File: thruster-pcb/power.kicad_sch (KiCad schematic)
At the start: 18 parts, among them J301 Molex_Pico-SPOX_Horizontal, J302 Molex_Pico-Lock-PLUS_Vertical, M301 Fan_5VDC_25x25x8mm, Q301 MOSFET-N-CH, U301 Switching_5V_500mA, U302 Linear_3.3V_1A

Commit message: tmc5160-usb -> thruster-pcb
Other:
- title: tmc5160-usb -> thruster-pcb
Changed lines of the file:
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@@
   (paper "A4")
   (title_block
-    (title "tmc5160-usb")
+    (title "thruster-pcb")
     (date "2024-05-10")
     (rev "1.0")
@@
     (pin "1")
     (instances
-      (project "tmc5160-usb"
+      (project "thruster-pcb"
         (path "/df2b2e89-e055-4140-95de-f1df723db034/c1dd8f61-494c-402f-8e59-08309c64fc3f"
           (reference "D303") (unit 1)
@@
     (pin "7")
     (instances
-      (project "tmc5160-usb"
+      (project "thruster-pcb"
         (path "/df2b2e89-e055-4140-95de-f1df723db034/c1dd8f61-494c-402f-8e59-08309c64fc3f"
           (reference "U302") (unit 1)
@@
     (pin "1")
     (instances
-      (project "tmc5160-usb"
+      (project "thruster-pcb"
         (path "/df2b2e89-e055-4140-95de-f1df723db034/c1dd8f61-494c-402f-8e59-08309c64fc3f"
           (reference "#FLG0303") (unit 1)
@@
     (pin "1")
     (instances
-      (project "tmc5160-usb"
+      (project "thruster-pcb"
         (path "/df2b2e89-e055-4140-95de-f1df723db034/c1dd8f61-494c-402f-8e59-08309c64fc3f"
           (reference "J302") (unit 1)
@@
     (pin "1")
     (instances
-      (project "tmc5160-usb"
+      (project "thruster-pcb"
         (path "/df2b2e89-e055-4140-95de-f1df723db034/c1dd8f61-494c-402f-8e59-08309c64fc3f"
           (reference "C302") (unit 1)
@@
     (pin "1")
     (instances
-      (project "tmc5160-usb"
+      (project "thruster-pcb"
         (path "/df2b2e89-e055-4140-95de-f1df723db034/c1dd8f61-494c-402f-8e59-08309c64fc3f"
           (reference "L301") (unit 1)
@@
     (pin "1")
     (instances
-      (project "tmc5160-usb"
+      (project "thruster-pcb"
         (path "/df2b2e89-e055-4140-95de-f1df723db034/c1dd8f61-494c-402f-8e59-08309c64fc3f"
           (reference "R303") (unit 1)
@@
     (pin "1")
     (instances
-      (project "tmc5160-usb"
+      (project "thruster-pcb"
         (path "/df2b2e89-e055-4140-95de-f1df723db034/c1dd8f61-494c-402f-8e59-08309c64fc3f"
           (reference "J301") (unit 1)
@@
     (pin "1")
     (instances
-      (project "tmc5160-usb"
+      (project "thruster-pcb"
         (path "/df2b2e89-e055-4140-95de-f1df723db034/c1dd8f61-494c-402f-8e59-08309c64fc3f"
           (reference "C304") (unit 1)
@@
     (pin "1")
     (instances
-      (project "tmc5160-usb"
+      (project "thruster-pcb"
         (path "/df2b2e89-e055-4140-95de-f1df723db034/c1dd8f61-494c-402f-8e59-08309c64fc3f"
           (reference "C301") (unit 1)
@@
     (pin "1")
     (instances
-      (project "tmc5160-usb"
+      (project "thruster-pcb"
         (path "/df2b2e89-e055-4140-95de-f1df723db034/c1dd8f61-494c-402f-8e59-08309c64fc3f"
           (reference "D301") (unit 1)
@@
     (pin "1")
     (instances
-      (project "tmc5160-usb"
+      (project "thruster-pcb"
         (path "/df2b2e89-e055-4140-95de-f1df723db034/c1dd8f61-494c-402f-8e59-08309c64fc3f"
           (reference "D302") (unit 1)
@@
     (pin "1")
     (instances
-      (project "tmc5160-usb"
+      (project "thruster-pcb"
         (path "/df2b2e89-e055-4140-95de-f1df723db034/c1dd8f61-494c-402f-8e59-08309c64fc3f"
           (reference "C305") (unit 1)
@@
     (pin "1")
     (instances
-      (project "tmc5160-usb"
+      (project "thruster-pcb"
         (path "/df2b2e89-e055-4140-95de-f1df723db034/c1dd8f61-494c-402f-8e59-08309c64fc3f"
           (reference "#FLG0302") (unit 1)
@@
     (pin "2")
     (instances
-      (project "tmc5160-usb"
+      (project "thruster-pcb"
         (path "/df2b2e89-e055-4140-95de-f1df723db034/c1dd8f61-494c-402f-8e59-08309c64fc3f"
           (reference "R302") (unit 1)
@@
     (pin "1")
     (instances
-      (project "tmc5160-usb"
+      (project "thruster-pcb"
         (path "/df2b2e89-e055-4140-95de-f1df723db034/c1dd8f61-494c-402f-8e59-08309c64fc3f"
           (reference "#FLG0301") (unit 1)
@@
     (pin "1")
     (instances
-      (project "tmc5160-usb"
+      (project "thruster-pcb"
         (path "/df2b2e89-e055-4140-95de-f1df723db034/c1dd8f61-494c-402f-8e59-08309c64fc3f"
           (reference "R301") (unit 1)
@@
     (pin "4")
     (instances
-      (project "tmc5160-usb"
+      (project "thruster-pcb"
         (path "/df2b2e89-e055-4140-95de-f1df723db034/c1dd8f61-494c-402f-8e59-08309c64fc3f"
           (reference "U301") (unit 1)
@@
     (pin "3")
     (instances
-      (project "tmc5160-usb"
+      (project "thruster-pcb"
         (path "/df2b2e89-e055-4140-95de-f1df723db034/c1dd8f61-494c-402f-8e59-08309c64fc3f"
           (reference "Q301") (unit 1)
@@
     (pin "2")
     (instances
-      (project "tmc5160-usb"
+      (project "thruster-pcb"
         (path "/df2b2e89-e055-4140-95de-f1df723db034/c1dd8f61-494c-402f-8e59-08309c64fc3f"
           (reference "M301") (unit 1)
@@
     (pin "1")
     (instances
-      (project "tmc5160-usb"
+      (project "thruster-pcb"
         (path "/df2b2e89-e055-4140-95de-f1df723db034/c1dd8f61-494c-402f-8e59-08309c64fc3f"
           (reference "C303") (unit 1)

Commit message: Add reference files
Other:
- company: Howard Hughes Medical Institute -> Mechatronic Magic
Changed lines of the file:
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@@
   (title_block
     (title "thruster-pcb")
-    (date "2024-05-10")
+    (date "2025-01-04")
     (rev "1.0")
-    (company "Howard Hughes Medical Institute")
+    (company "Mechatronic Magic")
   )
   (no_connect (at 163.83 68.58))

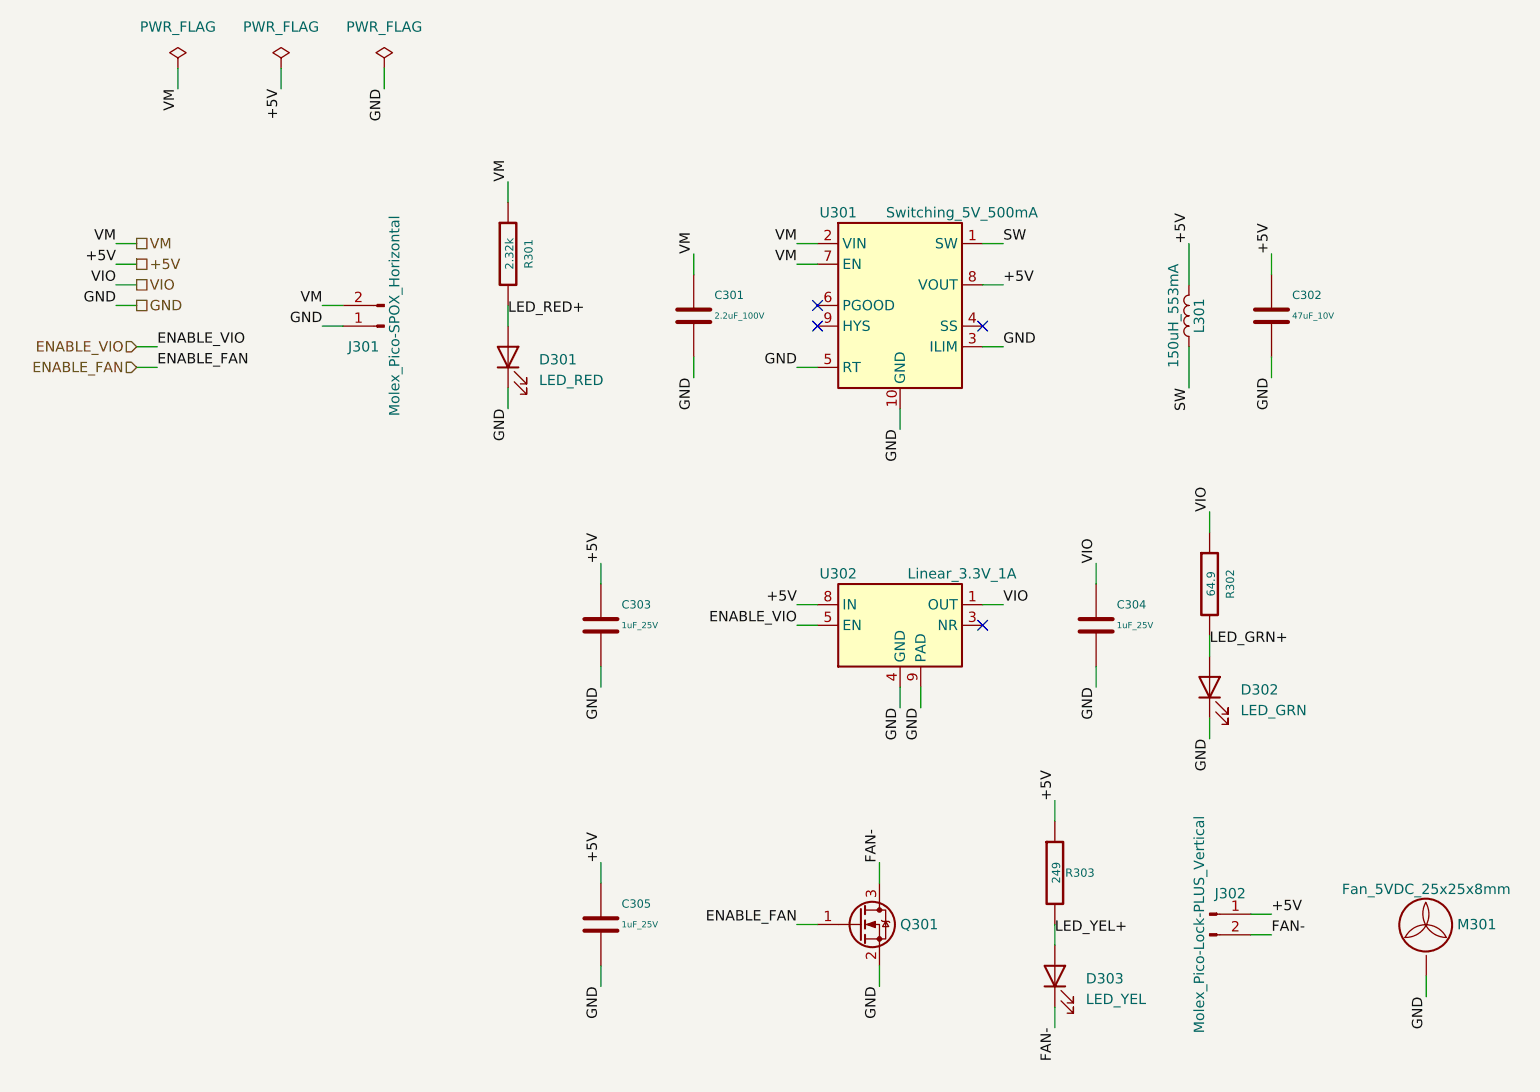
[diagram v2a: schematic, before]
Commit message: Use PCA9685 and nRF52
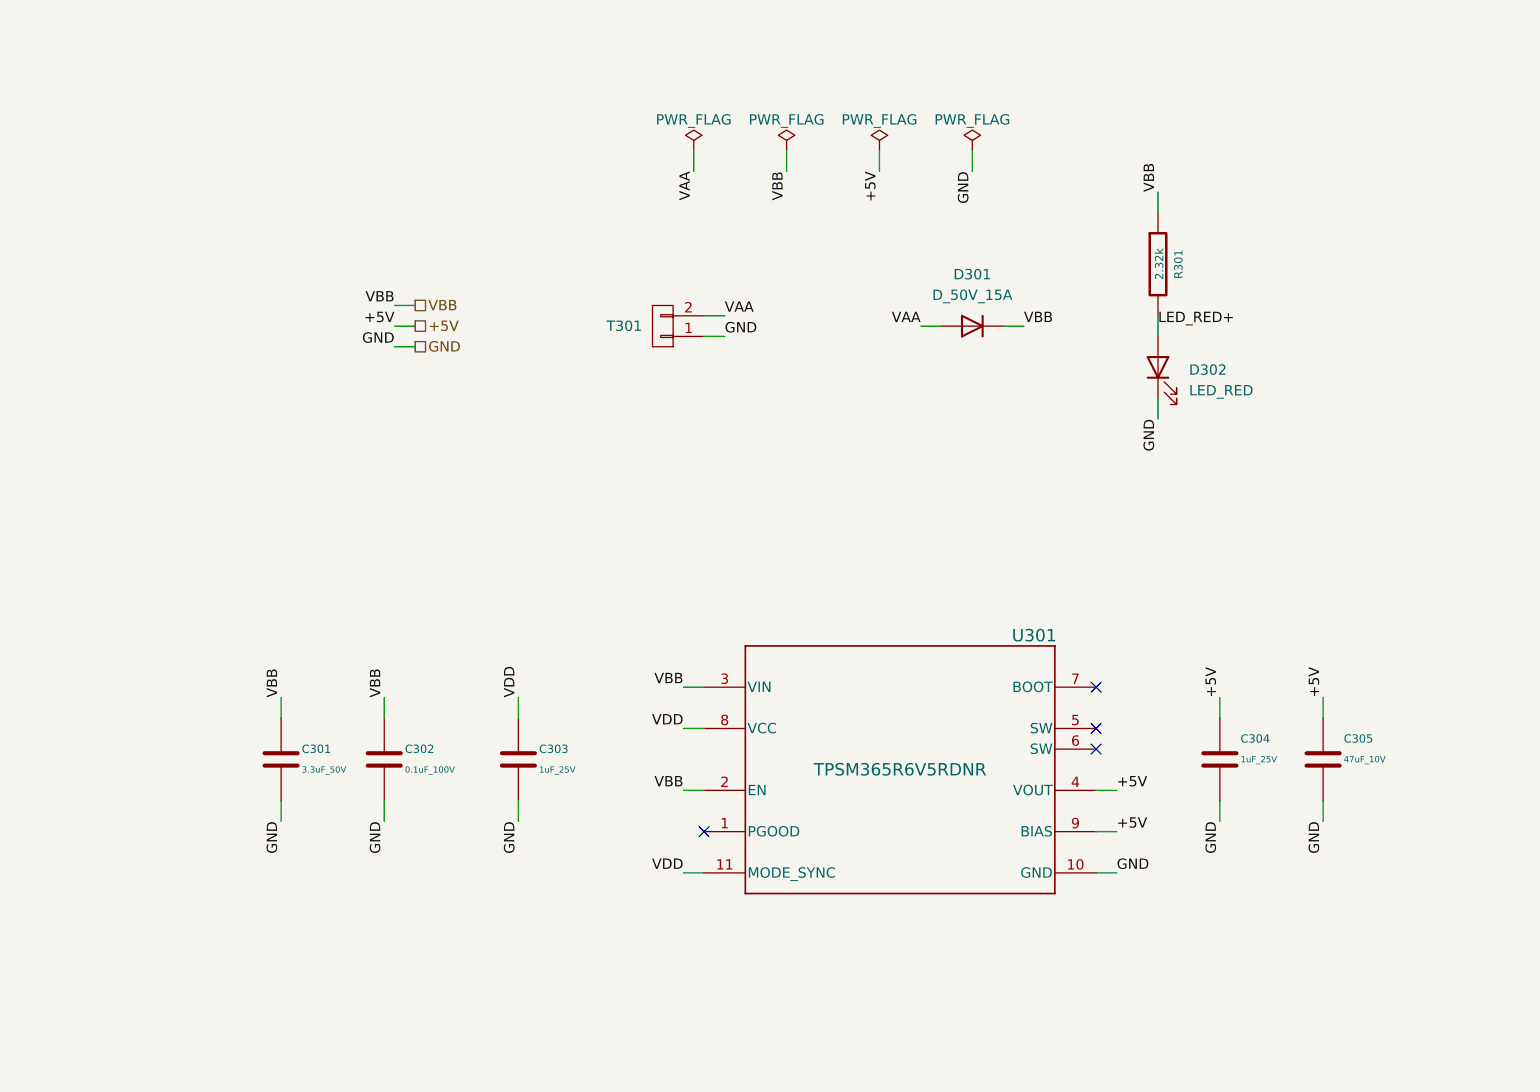
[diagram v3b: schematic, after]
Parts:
- removed C301: 2.2uF_100V, Janelia:C_0805_2012Metric, symbol Janelia:C_2.2uF_100V_0805
- removed C302: 47uF_10V, Janelia:C_0805_2012Metric, symbol Janelia:C_47uF_10V_0805
- removed C305: 1uF_25V, Janelia:C_0402_1005Metric, symbol Janelia:C_1uF_25V_0402
- removed D301: LED_RED, Janelia:LED_0402-1005_KNB, symbol Janelia:LED_KNB_20mA_RED_1.95V_0402
- removed D302: LED_GRN, Janelia:LED_0402-1005_KNB, symbol Janelia:LED_KNB_20mA_GRN_2.1V_0402
- removed D303: LED_YEL, Janelia:LED_0402-1005_KNB, symbol Janelia:LED_KNB_20mA_YEL_2V_0402
- removed J301: Molex_Pico-SPOX_Horizontal, Janelia:Molex_Pico-SPOX-87438_1x02-P1.5mm_Horizontal, symbol Janelia:Conn_01x02_P1.5mm_Molex_Pico-SPOX-87438_Horizontal
- removed J302: Molex_Pico-Lock-PLUS_Vertical, Janelia:Molex_Micro-Lock-PLUS-505568_1x02_P1.25mm_Vertical, symbol Janelia:Conn_01x02_P1.25mm_Molex_Micro-Lock-PLUS-505568_Vertical
- removed L301: 150uH_553mA, Janelia:IND_CB_SD25, symbol Janelia:L_150uH_553mA
- removed M301: Fan_5VDC_25x25x8mm, Janelia:FAN_5VDC_25x25x8mm, symbol Janelia:Fan_5VDC_25x25x8mm
- removed Q301: MOSFET-N-CH, Janelia:XFDFN-3, symbol Janelia:MOSFET-N-CH-EN-CSD17483F4
- removed R302: 64.9, Janelia:R_0402_1005Metric, symbol Janelia:R_64.9_0.1W_0402
- removed R303: 249, Janelia:R_0402_1005Metric, symbol Janelia:R_249_0.06W_0402
- removed U301: Switching_5V_500mA, Janelia:Texas_S-PVSON-N10_ThermalVias, symbol Janelia:Regulator_Switching_5V_500mA_LM5166X
- removed U302: Linear_3.3V_1A, Janelia:TPS737Q1, symbol Janelia:Regulator_Linear_3.3V_1A_5.5Vin_TPS73733QDRBRQ1
- added C301: 3.3uF_50V, Janelia:C_1210_3225Metric, symbol Janelia:C_3.3uF_50V_1210
- added C302: 0.1uF_100V, Janelia:C_0402_1005Metric, symbol Janelia:C_0.1uF_100V_0402
- added C305: 47uF_10V, Janelia:C_0805_2012Metric, symbol Janelia:C_47uF_10V_0805
- added D301: D_50V_15A, Janelia:POWERDI5_DIO, symbol Janelia:D_50V_15A
- added D302: LED_RED, Janelia:LED_0402-1005_KNB, symbol Janelia:LED_KNB_20mA_RED_1.95V_0402
- added T301: TERM_BLK_HDR_2POS_90DEG_0.2IN, Janelia:PHOENIX_1757242, symbol Janelia:TERM_BLK_HDR_2POS_90DEG_0.2IN
- added U301: TPSM365R6V5RDNR, Janelia:RDN0011A-MFG, symbol Janelia:TPSM365R6V5RDNR
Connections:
- net VIO is gone; now on net +5V: C304.1
- net +5V: now also C305.1, U301.4 (VOUT), U301.9 (BIAS); no longer C303.1
- net GND: now also C301.2, C302.2, C305.2, D302.1 (K), T301.1 (P1), U301.10 (GND)
- net LED_RED+: now also D302.2 (A)
- net VM renamed VBB
- net VBB: now also C301.1, C302.1, D301.1 (K), U301.2 (EN), U301.3 (VIN)
- new net VAA: D301.2 (A), T301.2 (P2)
- new net VDD: C303.1, U301.11 (MODE_SYNC), U301.8 (VCC)

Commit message: Initial components
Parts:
- removed D301: D_50V_15A, Janelia:POWERDI5_DIO, symbol Janelia:D_50V_15A
- removed D302: LED_RED, Janelia:LED_0402-1005_KNB, symbol Janelia:LED_KNB_20mA_RED_1.95V_0402
- removed R301: 2.32k, Janelia:R_0805_2012Metric, symbol Janelia:R_2.32k_1W_0805
- removed T301: TERM_BLK_HDR_2POS_90DEG_0.2IN, Janelia:PHOENIX_1757242, symbol Janelia:TERM_BLK_HDR_2POS_90DEG_0.2IN
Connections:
- net VBB renamed +6V

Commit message: Add sheets
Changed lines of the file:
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@@
     (stroke (width 0) (type default))
   )
-  (wire (pts (xy 93.98 71.12) (xy 91.44 71.12))
+  (wire (pts (xy 91.44 71.12) (xy 93.98 71.12))
     (stroke (width 0) (type default))
   )
@@
     (stroke (width 0) (type default))
   )
-  (wire (pts (xy 93.98 68.58) (xy 91.44 68.58))
+  (wire (pts (xy 91.44 68.58) (xy 93.98 68.58))
     (stroke (width 0) (type default))
   )
@@
     (stroke (width 0) (type default))
   )
-  (wire (pts (xy 93.98 66.04) (xy 91.44 66.04))
+  (wire (pts (xy 91.44 66.04) (xy 93.98 66.04))
     (stroke (width 0) (type default))
   )
@@
     (effects (font (size 1.27 1.27)) (justify left bottom))
   )
-  (label "+6V" (at 91.44 66.04 180) (fields_autoplaced)
-    (effects (font (size 1.27 1.27)) (justify right bottom))
+  (label "+6V" (at 93.98 66.04 0) (fields_autoplaced)
+    (effects (font (size 1.27 1.27)) (justify left bottom))
   )
   (label "VDD" (at 127 135.89 180) (fields_autoplaced)
@@
     (effects (font (size 1.27 1.27)) (justify right bottom))
   )
-  (label "GND" (at 91.44 71.12 180) (fields_autoplaced)
-    (effects (font (size 1.27 1.27)) (justify right bottom))
+  (label "GND" (at 93.98 71.12 0) (fields_autoplaced)
+    (effects (font (size 1.27 1.27)) (justify left bottom))
   )
   (label "GND" (at 77.47 129.54 270) (fields_autoplaced)
     (effects (font (size 1.27 1.27)) (justify right bottom))
   )
-  (label "+5V" (at 91.44 68.58 180) (fields_autoplaced)
-    (effects (font (size 1.27 1.27)) (justify right bottom))
+  (label "+5V" (at 93.98 68.58 0) (fields_autoplaced)
+    (effects (font (size 1.27 1.27)) (justify left bottom))
   )
   (label "GND" (at 106.68 129.54 270) (fields_autoplaced)
@@
     (effects (font (size 1.27 1.27)) (justify right bottom))
   )
-  (hierarchical_label "+5V" (shape passive) (at 93.98 68.58 0) (fields_autoplaced)
-    (effects (font (size 1.27 1.27)) (justify left))
-  )
-  (hierarchical_label "GND" (shape passive) (at 93.98 71.12 0) (fields_autoplaced)
-    (effects (font (size 1.27 1.27)) (justify left))
-  )
-  (hierarchical_label "+6V" (shape passive) (at 93.98 66.04 0) (fields_autoplaced)
-    (effects (font (size 1.27 1.27)) (justify left))
+  (hierarchical_label "+5V" (shape passive) (at 91.44 68.58 180) (fields_autoplaced)
+    (effects (font (size 1.27 1.27)) (justify right))
+  )
+  (hierarchical_label "GND" (shape passive) (at 91.44 71.12 180) (fields_autoplaced)
+    (effects (font (size 1.27 1.27)) (justify right))
+  )
+  (hierarchical_label "+6V" (shape passive) (at 91.44 66.04 180) (fields_autoplaced)
+    (effects (font (size 1.27 1.27)) (justify right))
   )
   (symbol (lib_id "Janelia:C_1uF_25V_0402") (at 106.68 121.92 0) (unit 1)
@@
   (symbol (lib_id "power:PWR_FLAG") (at 162.56 46.99 0) (unit 1)
     (in_bom yes) (on_board yes) (dnp no)
-    (property "Reference" "#FLG0305" (at 162.56 45.085 0)
+    (property "Reference" "#FLG0303" (at 162.56 45.085 0)
       (effects (font (size 1.27 1.27)) hide)
     )
@@
       (project "thruster-pcb"
         (path "/df2b2e89-e055-4140-95de-f1df723db034/c1dd8f61-494c-402f-8e59-08309c64fc3f"
-          (reference "#FLG0305") (unit 1)
+          (reference "#FLG0303") (unit 1)
         )
       )
@@
   (symbol (lib_id "power:PWR_FLAG") (at 139.7 46.99 0) (unit 1)
     (in_bom yes) (on_board yes) (dnp no)
-    (property "Reference" "#FLG0302" (at 139.7 45.085 0)
+    (property "Reference" "#FLG0301" (at 139.7 45.085 0)
       (effects (font (size 1.27 1.27)) hide)
     )
@@
       (project "thruster-pcb"
         (path "/df2b2e89-e055-4140-95de-f1df723db034/c1dd8f61-494c-402f-8e59-08309c64fc3f"
-          (reference "#FLG0302") (unit 1)
+          (reference "#FLG0301") (unit 1)
         )
       )
@@
   (symbol (lib_id "power:PWR_FLAG") (at 151.13 46.99 0) (unit 1)
     (in_bom yes) (on_board yes) (dnp no)
-    (property "Reference" "#FLG0304" (at 151.13 45.085 0)
+    (property "Reference" "#FLG0302" (at 151.13 45.085 0)
       (effects (font (size 1.27 1.27)) hide)
     )
@@
       (project "thruster-pcb"
         (path "/df2b2e89-e055-4140-95de-f1df723db034/c1dd8f61-494c-402f-8e59-08309c64fc3f"
-          (reference "#FLG0304") (unit 1)
-        )
-      )
+          (reference "#FLG0302") (unit 1)
+        )
+      )
